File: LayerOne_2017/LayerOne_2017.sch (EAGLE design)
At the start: 107 parts, among them IC1 STM32F446_LQFP64LQFP64, IC2 REG1117, J1 SPI_TFT_DISPLAY, Q1 2N2222, Q2 MMBT2222A, U1 SN65HVD235DR, U2 SN65HVD235DR, U4 SDCARD, U5 FERRITE0805, X1 STEREOJACK, X2 MINI-USB-32005-301

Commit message: third rev
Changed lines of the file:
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@@
 <part name="R10" library="SparkFun-Passives" deviceset="RESISTOR" device="0805-RES" value="100"/>
 <part name="R11" library="SparkFun-Passives" deviceset="RESISTOR" device="0805-RES" value="10K"/>
-<part name="U$21" library="microbuilder" deviceset="3.3V" device=""/>
 <part name="U3" library="microbuilder" deviceset="DISP_LCD_TM022HDH26" device=""/>
 <part name="U$6" library="microbuilder" deviceset="3.3V" device=""/>
@@
 <instance part="R10" gate="G$1" x="30.48" y="25.4"/>
 <instance part="R11" gate="G$1" x="38.1" y="15.24" rot="R90"/>
-<instance part="U$21" gate="G$1" x="20.32" y="53.34"/>
 <instance part="U3" gate="G$1" x="124.46" y="43.18"/>
 <instance part="U$6" gate="G$1" x="81.28" y="43.18"/>
@@
 <wire x1="38.1" y1="25.4" x2="45.72" y2="25.4" width="0.1524" layer="91"/>
 <wire x1="38.1" y1="20.32" x2="38.1" y2="25.4" width="0.1524" layer="91"/>
+<junction x="38.1" y="25.4"/>
 </segment>
 </net>
@@
 <wire x1="-15.24" y1="10.16" x2="-15.24" y2="7.62" width="0.1524" layer="91"/>
 <wire x1="-15.24" y1="7.62" x2="-22.86" y2="7.62" width="0.1524" layer="91"/>
+<junction x="-22.86" y="7.62"/>
 </segment>
 <segment>
@@
 <pinref part="R21" gate="G$1" pin="2"/>
 <wire x1="-2.54" y1="-50.8" x2="0" y2="-50.8" width="0.1524" layer="91"/>
-<wire x1="0" y1="-50.8" x2="0" y2="-53.34" width="0.1524" layer="91"/>
 <wire x1="-2.54" y1="-48.26" x2="-2.54" y2="-50.8" width="0.1524" layer="91"/>
 <pinref part="R22" gate="G$1" pin="2"/>
@@
 <wire x1="7.62" y1="-50.8" x2="0" y2="-50.8" width="0.1524" layer="91"/>
 <wire x1="0" y1="-50.8" x2="0" y2="-53.34" width="0.1524" layer="91"/>
+<junction x="-2.54" y="-50.8"/>
+<junction x="0" y="-50.8"/>
 </segment>
 <segment>
@@
 <wire x1="-25.4" y1="15.24" x2="-33.02" y2="15.24" width="0.1524" layer="91"/>
 <wire x1="-25.4" y1="15.24" x2="-25.4" y2="25.4" width="0.1524" layer="91"/>
+<junction x="-25.4" y="15.24"/>
+<junction x="-22.86" y="15.24"/>
 </segment>
 </net>
@@
 <pinref part="VBAT" gate="G$1" pin="TP"/>
 <wire x1="50.8" y1="12.7" x2="50.8" y2="22.86" width="0.1524" layer="91"/>
+<junction x="50.8" y="12.7"/>
 </segment>
 </net>
@@
 <wire x1="119.38" y1="86.36" x2="124.46" y2="86.36" width="0.1524" layer="91"/>
 <wire x1="119.38" y1="93.98" x2="119.38" y2="86.36" width="0.1524" layer="91"/>
+<junction x="119.38" y="86.36"/>
 </segment>
 </net>
@@
 <wire x1="17.78" y1="81.28" x2="17.78" y2="86.36" width="0.1524" layer="91"/>
 <junction x="17.78" y="86.36"/>
+<label x="2.54" y="86.36" size="1.778" layer="95" font="fixed" rot="R180" xref="yes"/>
 </segment>
 </net>
@@
 <pinref part="R12" gate="G$1" pin="2"/>
 <wire x1="60.96" y1="43.18" x2="60.96" y2="25.4" width="0.1524" layer="91"/>
-</segment>
-</net>
+<junction x="38.1" y="43.18"/>
+<junction x="50.8" y="43.18"/>
+<junction x="60.96" y="43.18"/>
+</segment>
+</net>

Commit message: fixed usb moved reset button.
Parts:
- C2, C3: value 20pF -> 18pF
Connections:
- net D+: now also CN1.D+; no longer CN1.D-
- net D-: now also CN1.D-; no longer CN1.D+
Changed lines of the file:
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@@
 <part name="U$8" library="adafruit" deviceset="FIDUCIAL" device=""/>
 <part name="U$9" library="adafruit" deviceset="FIDUCIAL" device=""/>
-<part name="C2" library="SparkFun-Passives" deviceset="CAP" device="0805" value="20pF"/>
-<part name="C3" library="SparkFun-Passives" deviceset="CAP" device="0805" value="20pF"/>
+<part name="C2" library="SparkFun-Passives" deviceset="CAP" device="0805" value="18pF"/>
+<part name="C3" library="SparkFun-Passives" deviceset="CAP" device="0805" value="18pF "/>
 <part name="IC2" library="burr-brown" deviceset="REG1117" device=""/>
 <part name="U$10" library="microbuilder" deviceset="GND" device=""/>
@@
 </segment>
 <segment>
-<wire x1="210.82" y1="43.18" x2="210.82" y2="45.72" width="0.1524" layer="91"/>
-<label x="210.82" y="45.72" size="1.778" layer="95" rot="R90" xref="yes"/>
-<pinref part="CN1" gate="G$1" pin="D+"/>
+<pinref part="CN1" gate="G$1" pin="D-"/>
+<wire x1="208.28" y1="43.18" x2="208.28" y2="63.5" width="0.1524" layer="91"/>
 </segment>
 </net>
@@
 </segment>
 <segment>
-<wire x1="208.28" y1="43.18" x2="208.28" y2="63.5" width="0.1524" layer="91"/>
-<label x="208.28" y="63.5" size="1.778" layer="95" rot="R90" xref="yes"/>
-<pinref part="CN1" gate="G$1" pin="D-"/>
-</segment>
-</net>
+<pinref part="CN1" gate="G$1" pin="D+"/>
+<wire x1="210.82" y1="43.18" x2="210.82" y2="66.04" width="0.1524" layer="91"/>
+</segment>
+</net>

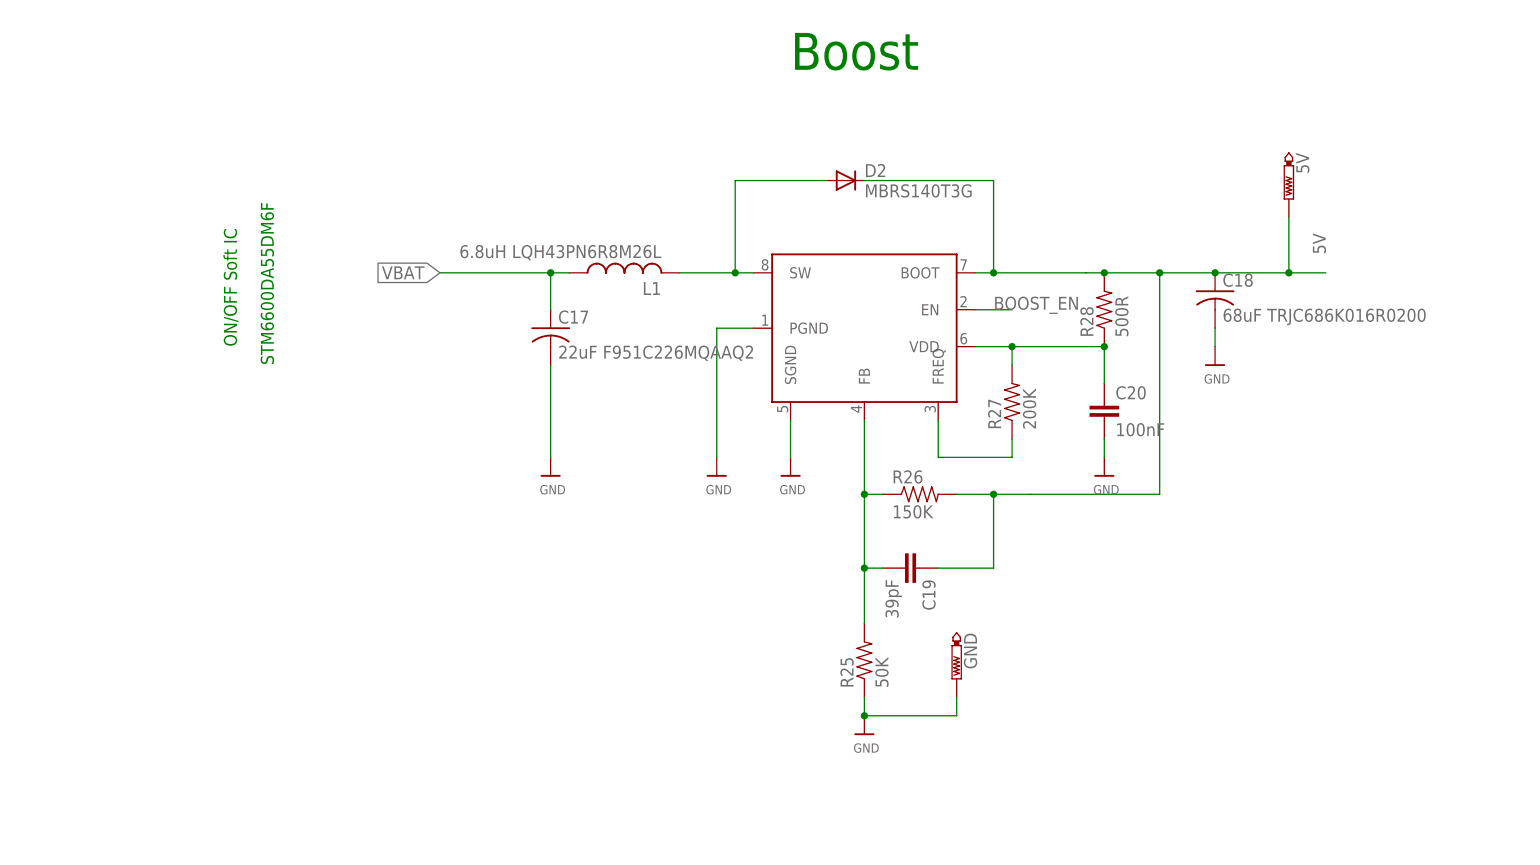
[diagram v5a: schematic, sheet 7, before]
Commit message: 
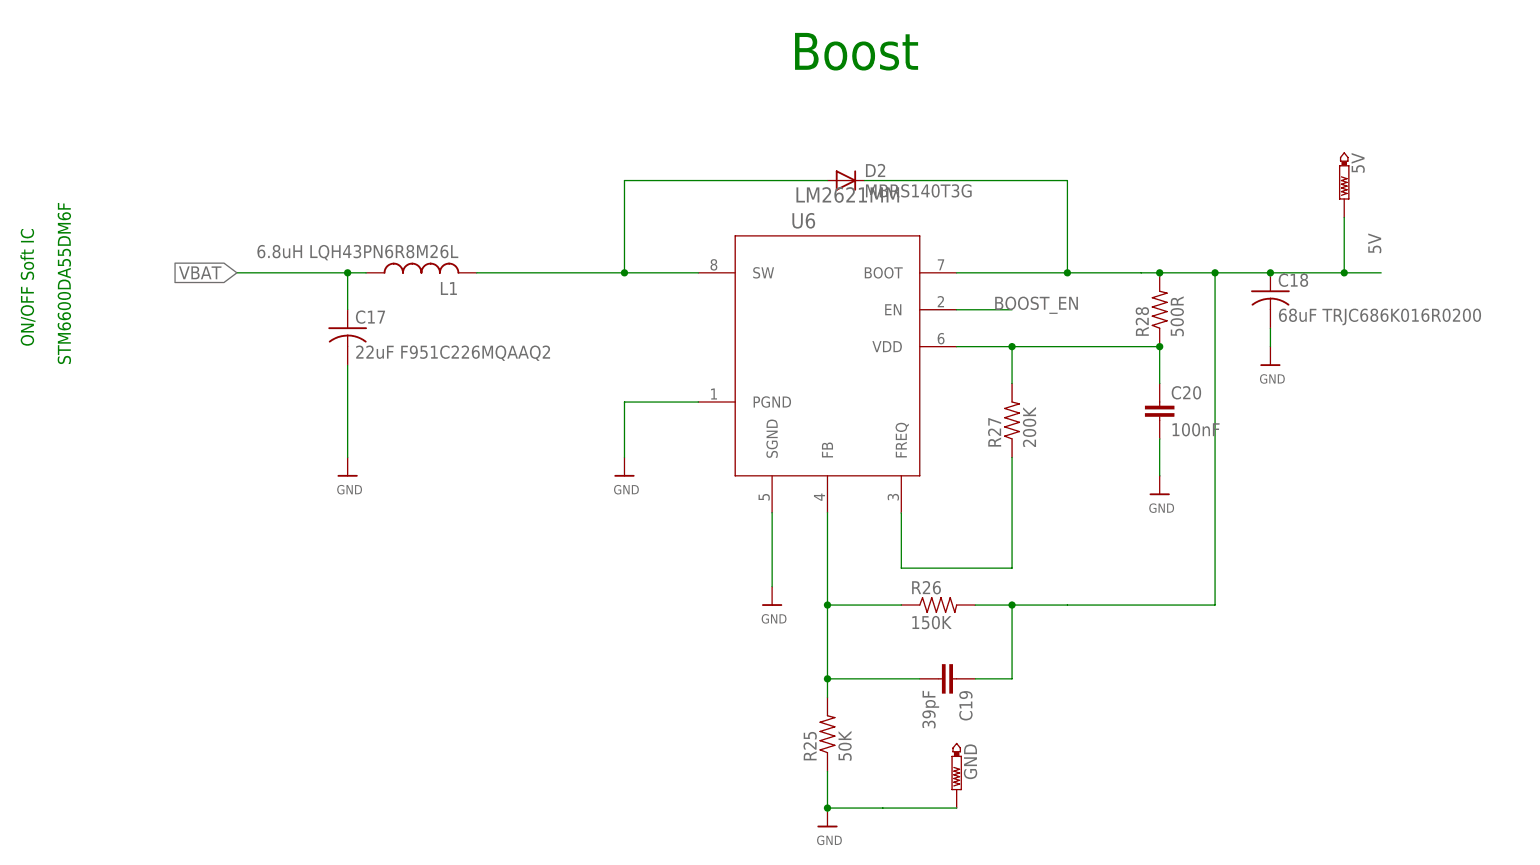
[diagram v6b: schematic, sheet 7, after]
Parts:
- removed U$30: TI-LM2621, LayerOne_2017:TI-LM2621
- added U6: LM2621MM, LM2621MM:LM2621MM
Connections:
- removed net N$30: D2.A, L1.2, U$30.SW
- removed net N$40: C19.2, R25.2, R26.1, U$30.FB
- removed net N$43: R27.1, U$30.FREQ
- removed net N$44: C20.1, R27.2, R28.1, U$30.VDD
- new net FB: C19.2, R25.2, R26.1, U6.FB
- new net FREQ: R27.1, U6.FREQ
- new net SW: D2.A, L1.2, U6.SW
- new net VDD: C20.1, R27.2, R28.1, U6.VDD
- net 5V: now also U6.BOOT; no longer U$30.BOOT
- net BOOST_EN: now also U6.EN; no longer U$30.EN
- net GND: now also U6.PGND, U6.SGND; no longer U$30.PGND, U$30.SGND
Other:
- moved on the sheet: 5V, C17, C18, C19, C20, GND, L1, R25, R26, R27, R28
